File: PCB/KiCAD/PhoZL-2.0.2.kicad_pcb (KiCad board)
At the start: 2 copper layers, 125.5 x 90.3 mm, 106 parts, among them J1 Conn_01x06_Female, J11 Conn_01x02, J14 Conn_01x06, J15 Conn_01x06, J2 Conn_01x02, J3 Conn_01x02, J4 Conn_01x01, J5 Rumble, J6 Conn_01x06, J8 USB_B_Micro, Q1 Q_NMOS_GSD, Q2 Q_PMOS_GDS, Q3 Q_NMOS_GSD, SW1 A, SW10 Dup, SW11 Dright, SW12 Ddown, SW2 B, SW3 X, SW4 Y, SW5 Start, SW6 L, SW7 R, SW8 ZR, SW8L ZL, SW9 Dleft, U1 MCP3002, U10 DRV5055A2xDBZxQ1, U11 DRV5055A2xDBZxQ1, U2 Stickbox_Assembly_Main, U3 MCP3002, U4 DRV5055A2xDBZxQ1, U5 Stickbox_Assembly_CStick, U6 AMS1117-3.3, U7 W25Q128JVS, U8 RP2040, U9 DRV5055A2xDBZxQ1, Y1 Crystal_GND24

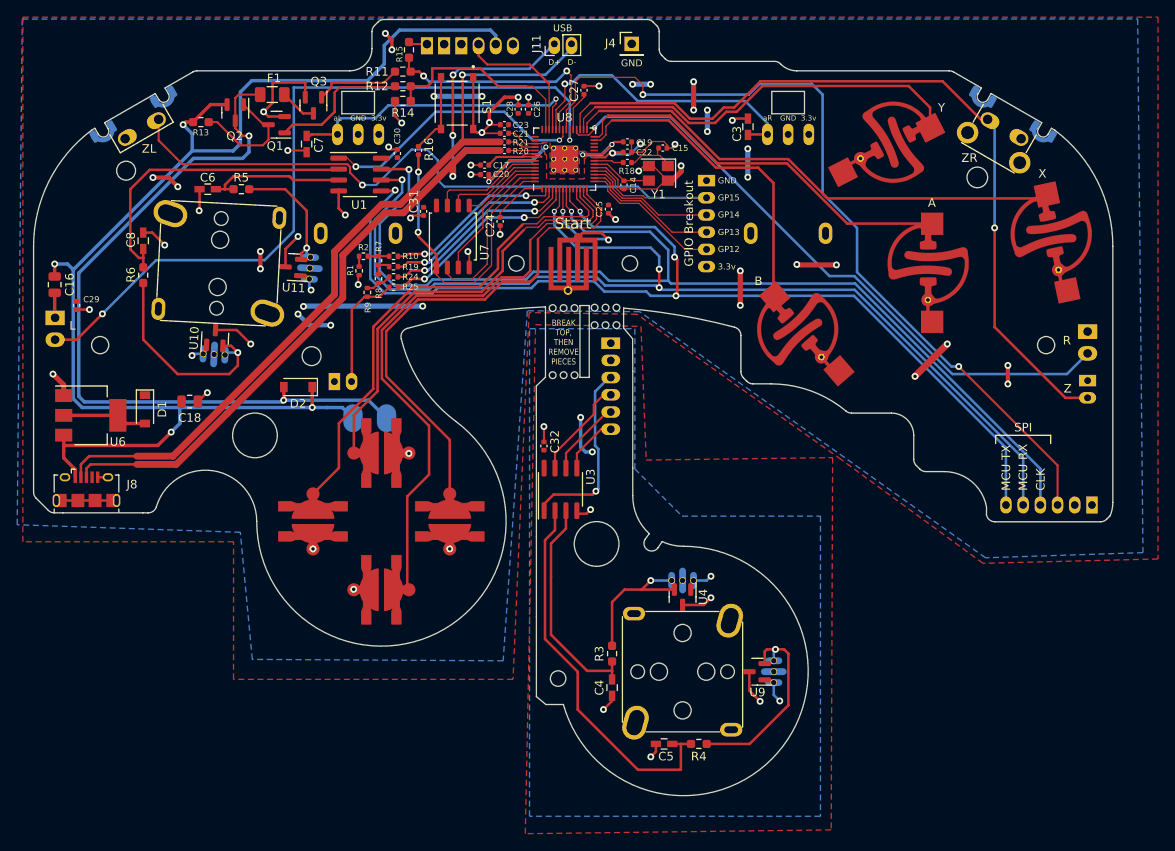
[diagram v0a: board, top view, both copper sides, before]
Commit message: 12-16-22 Changes
pcb has been redone on the newest version of the 2.0.2 pcb
(my dpad was added to the main pcb!)
gpio15 on zl changed to gpio12
removed the zl input from the GPIO breakout, instead going directly into the rp2040
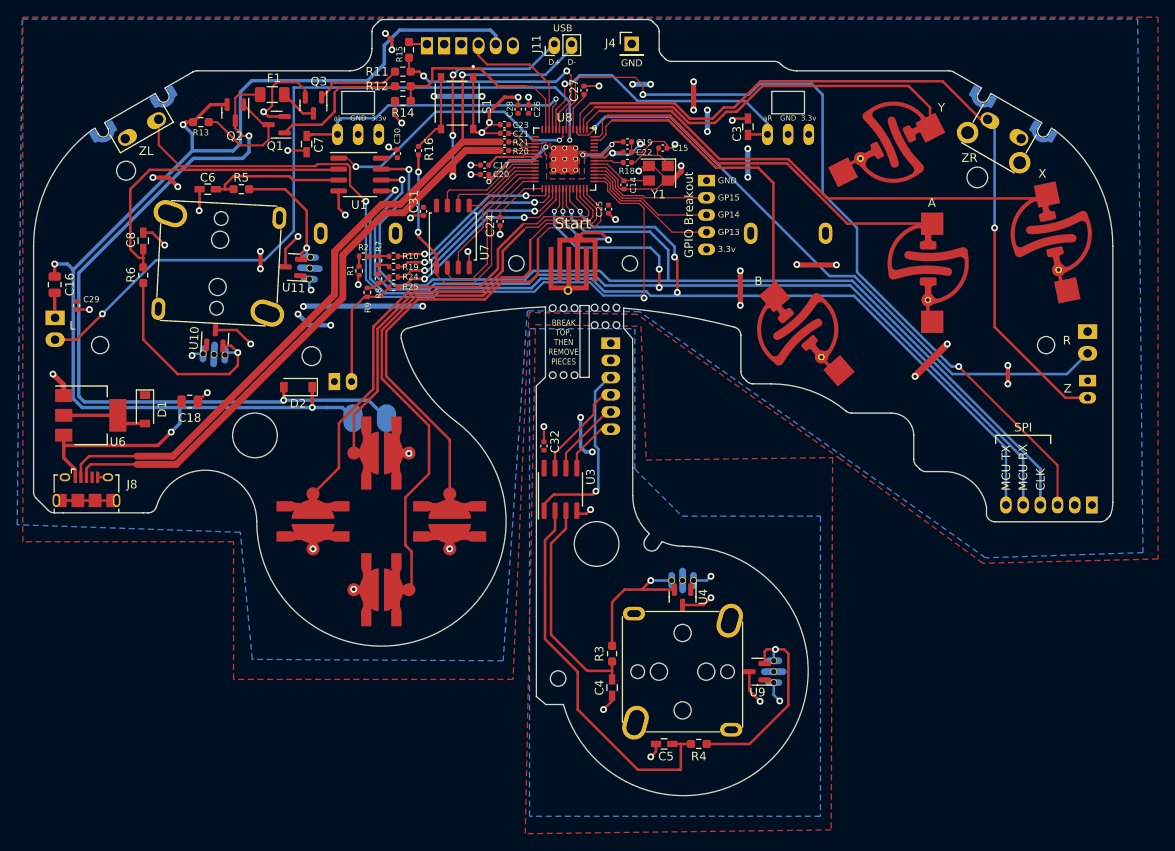
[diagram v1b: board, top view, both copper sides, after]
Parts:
- SW8: value ZR -> Z
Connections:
- J6 pad 2: /GPIO12 -> +3V3
- SW8L pad 2: /GPIO15 -> /GPIO12
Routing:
- net /GPIO12: track 17.0 -> 92.9 mm, vias 0 -> 2
- net /GPIO15: track 89.1 -> 15.0 mm, vias 1 -> 0
- net /Din: track 124.9 -> 125.7 mm
- net GND: track 138.4 -> 137.8 mm
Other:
- board text removed: "GP12"

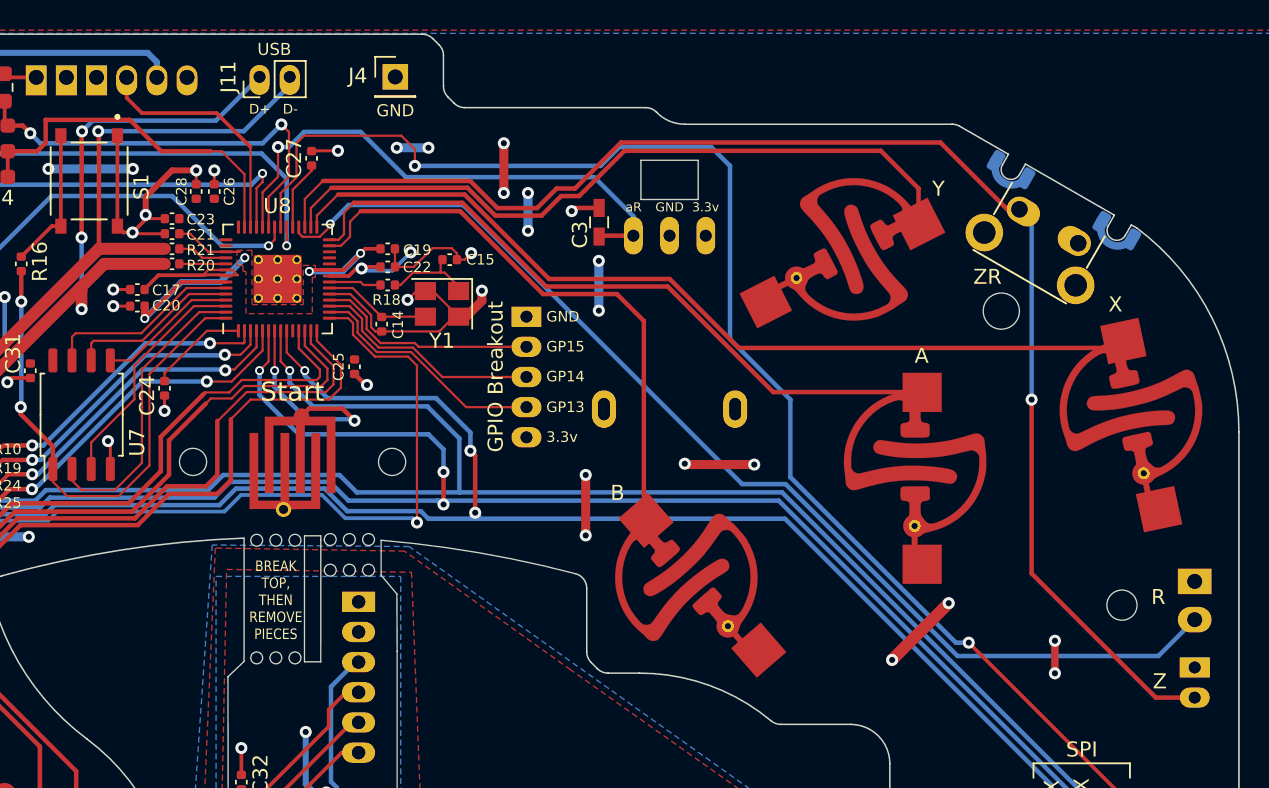
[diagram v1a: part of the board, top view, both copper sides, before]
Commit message: 12-20-22 Changes
slight updates to the silkscreen
USB Data + / - as well as the GND at the top of the PCB has been relocated
(Credit to Plants for the idea!)
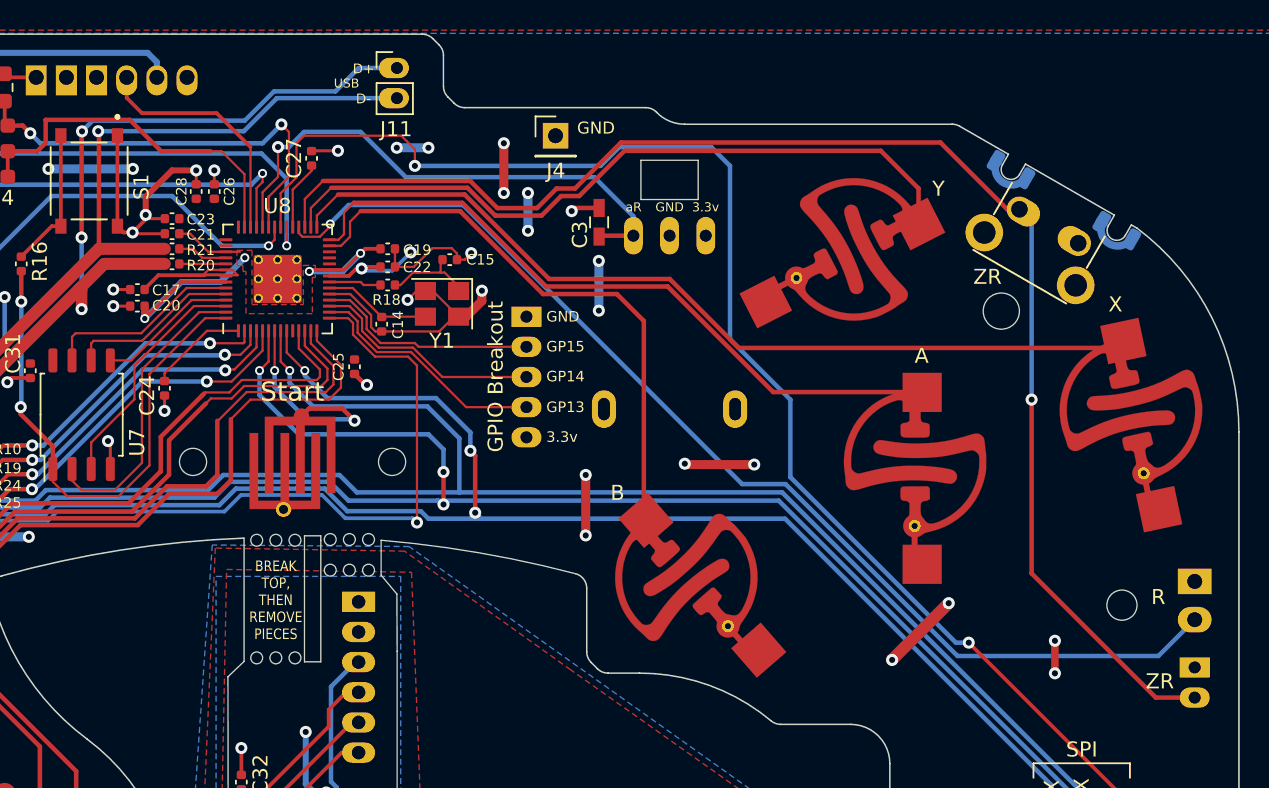
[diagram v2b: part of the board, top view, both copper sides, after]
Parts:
- moved J4 11.3 mm to (128.4, 29.6)
- moved J11 9.13 mm to (117.9, 25.0), turned to 0 degrees
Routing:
- net /USB_D+: track 93.9 -> 103.2 mm
- net /USB_D-: track 91.1 -> 97.3 mm
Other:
- board text removed: "Z"
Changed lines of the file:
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@@
   )
   (footprint "PhobGCC_2_0_0_footprints:PinHeader_1x01_P2.54mm_Vertical" (layer "F.Cu")
-    (at 117.8 25.6)
+    (at 128.43 29.55)
     (descr "Through hole straight pin header, 1x01, 2.54mm pitch, single row")
     (tags "Through hole pin header THT 1x01 2.54mm single row")
@@
     (property "Sheetname" "")
     (attr through_hole)
-    (fp_text reference "J4" (at -2.484 -0.073) (layer "F.SilkS")
+    (fp_text reference "J4" (at 0.02 2.28) (layer "F.SilkS")
       (effects (font (size 1 1) (thickness 0.15)))
     )
@@
     (fp_line (start 1.27 1.27) (end -1.27 1.27) (layer "F.Fab") (width 0.1))
     (fp_line (start -1.27 -0.635) (end -0.635 -1.27) (layer "F.Fab") (width 0.1))
-    (pad "1" thru_hole rect (at 0 0) (size 1.7 1.7) (drill 1) (layers *.Cu *.Mask)
+    (pad "1" thru_hole rect (at 0 -0.05) (size 1.7 1.7) (drill 1) (layers *.Cu *.Mask)
       (net 1 "GND") (pinfunction "Pin_1") (pintype "passive"))
     (model "${KICAD6_3DMODEL_DIR}/Connector_PinHeader_2.54mm.3dshapes/PinHeader_1x01_P2.54mm_Vertical.wrl" hide
@@
   )
   (footprint "PhobGCC_2_0_0_footprints:PinHeader_1x02_P2.00mm_Vertical" (layer "F.Cu")
-    (at 108.8 25.6 90)
+    (at 117.91 25.01)
     (descr "Through hole straight pin header, 1x02, 2.00mm pitch, single row")
     (tags "Through hole pin header THT 1x02 2.00mm single row")
@@
     (property "Sheetname" "")
     (attr through_hole)
-    (fp_text reference "J11" (at 0 -2.06 90) (layer "F.SilkS")
+    (fp_text reference "J11" (at -0.05 4.06) (layer "F.SilkS")
       (effects (font (size 1 1) (thickness 0.15)))
     )
-    (fp_text value "Conn_01x02" (at 0 4.06 90) (layer "F.Fab")
+    (fp_text value "Conn_01x02" (at 0 4.06) (layer "F.Fab")
       (effects (font (size 1 1) (thickness 0.15)))
     )
-    (fp_text user "${REFERENCE}" (at 0 1) (layer "F.Fab")
+    (fp_text user "${REFERENCE}" (at 0 1 90) (layer "F.Fab")
       (effects (font (size 1 1) (thickness 0.15)))
     )
@@
     (fp_line (start 1 3) (end -1 3) (layer "F.Fab") (width 0.1))
     (fp_line (start -0.5 -1) (end 1 -1) (layer "F.Fab") (width 0.1))
-    (pad "1" thru_hole oval (at 0 0 90) (size 2 1.35) (drill 0.8 (offset -0.2 0)) (layers *.Cu *.Mask)
+    (pad "1" thru_hole oval (at 0 0) (size 2 1.35) (drill 0.8 (offset -0.2 0)) (layers *.Cu *.Mask)
       (net 37 "/USB_D+") (pinfunction "Pin_1") (pintype "passive"))
-    (pad "2" thru_hole oval (at 0 2 90) (size 2 1.35) (drill 0.8 (offset -0.2 0)) (layers *.Cu *.Mask)
+    (pad "2" thru_hole oval (at 0 2) (size 2 1.35) (drill 0.8 (offset -0.2 0)) (layers *.Cu *.Mask)
       (net 38 "/USB_D-") (pinfunction "Pin_2") (pintype "passive"))
     (model "${KICAD6_3DMODEL_DIR}/Connector_PinHeader_2.00mm.3dshapes/PinHeader_1x02_P2.00mm_Vertical.wrl" hide
@@
     (effects (font (size 0.7 0.7) (thickness 0.15)) (justify right mirror))
   )
-  (gr_text "Z" (at 168.5036 65.6844) (layer "B.SilkS")
+  (gr_text "ZR" (at 168.5036 65.6844) (layer "B.SilkS")
     (effects (font (size 1 1) (thickness 0.15)) (justify mirror))
   )
@@
     (effects (font (size 0.6 0.6) (thickness 0.1)))
   )
-  (gr_text "D-" (at 110.8436 27.7368) (layer "F.SilkS")
+  (gr_text "D-" (at 115.69 27.05) (layer "F.SilkS")
     (effects (font (size 0.65 0.65) (thickness 0.15)))
   )
@@
     (effects (font (size 1 1) (thickness 0.15)) (justify left))
   )
-  (gr_text "D+" (at 108.8136 27.7368) (layer "F.SilkS")
+  (gr_text "D+" (at 115.69 25.06) (layer "F.SilkS")
     (effects (font (size 0.65 0.65) (thickness 0.15)))
   )
@@
     (effects (font (size 1 1) (thickness 0.15)) (justify left))
   )
-  (gr_text "Z" (at 168.5036 65.6844) (layer "F.SilkS")
+  (gr_text "ZR" (at 168.5036 65.6844) (layer "F.SilkS")
     (effects (font (size 1 1) (thickness 0.15)))
   )
@@
     (effects (font (size 0.7 0.7) (thickness 0.15)) (justify left))
   )
-  (gr_text "GND" (at 117.8052 27.8384) (layer "F.SilkS")
+  (gr_text "GND" (at 131.11 28.99) (layer "F.SilkS")
     (effects (font (size 0.8 0.8) (thickness 0.15)))
   )
@@
     (effects (font (size 1 1) (thickness 0.15)))
   )
-  (gr_text "USB" (at 109.7788 23.7744) (layer "F.SilkS")
-    (effects (font (size 0.8 0.8) (thickness 0.15)))
+  (gr_text "USB" (at 114.57 26.03) (layer "F.SilkS")
+    (effects (font (size 0.6 0.6) (thickness 0.1125)))
   )
   (gr_text "SPI" (at 163.322 70.2056) (layer "F.SilkS")
@@
   (segment (start 97 41) (end 97 36.25) (width 0.3) (layer "B.Cu") (net 37))
   (segment (start 97.028 29.21) (end 97.738 28.5) (width 0.3) (layer "B.Cu") (net 37))
-  (segment (start 105.9 28.5) (end 108.8 25.6) (width 0.3) (layer "B.Cu") (net 37))
-  (segment (start 97.738 28.5) (end 105.9 28.5) (width 0.3) (layer "B.Cu") (net 37))
+  (segment (start 107.820404 28.5) (end 109.760404 26.56) (width 0.3) (layer "B.Cu") (net 37))
+  (segment (start 109.760404 26.56) (end 113.83 26.56) (width 0.3) (layer "B.Cu") (net 37))
+  (segment (start 113.83 26.56) (end 115.38 25.01) (width 0.3) (layer "B.Cu") (net 37))
+  (segment (start 97.738 28.5) (end 107.820404 28.5) (width 0.3) (layer "B.Cu") (net 37))
+  (segment (start 115.38 25.01) (end 117.91 25.01) (width 0.3) (layer "B.Cu") (net 37))
   (segment (start 64.45452 73.54548) (end 83.25 54.75) (width 0.8) (layer "F.Cu") (net 38))
   (segment (start 60.25 73.54548) (end 64.45452 73.54548) (width 0.8) (layer "F.Cu") (net 38))
@@
   (segment (start 54.70452 73.54548) (end 60.25 73.54548) (width 0.3) (layer "F.Cu") (net 38))
   (via (at 98.1 29.2) (size 0.8) (drill 0.4) (layers "F.Cu" "B.Cu") (net 38))
-  (segment (start 107.7568 29.2) (end 110.8 26.1568) (width 0.3) (layer "B.Cu") (net 38))
-  (segment (start 110.8 26.1568) (end 110.8 25.6) (width 0.3) (layer "B.Cu") (net 38))
   (segment (start 98.1 29.2) (end 107.7568 29.2) (width 0.3) (layer "B.Cu") (net 38))
+  (segment (start 107.7568 29.2) (end 109.9468 27.01) (width 0.3) (layer "B.Cu") (net 38))
+  (segment (start 109.9468 27.01) (end 117.91 27.01) (width 0.3) (layer "B.Cu") (net 38))
   (segment (start 93 37.52) (end 95.02 35.5) (width 0.25) (layer "F.Cu") (net 39))
   (segment (start 95.625 29.5) (end 95.625 35.5) (width 0.25) (layer "F.Cu") (net 39))

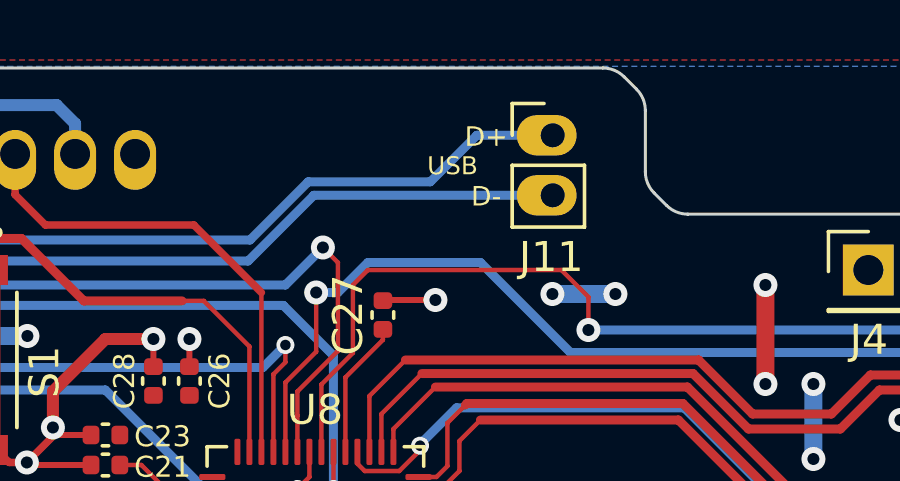
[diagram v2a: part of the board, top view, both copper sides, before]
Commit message: 12-23-22 Changes
updated dpad to match current phob 2
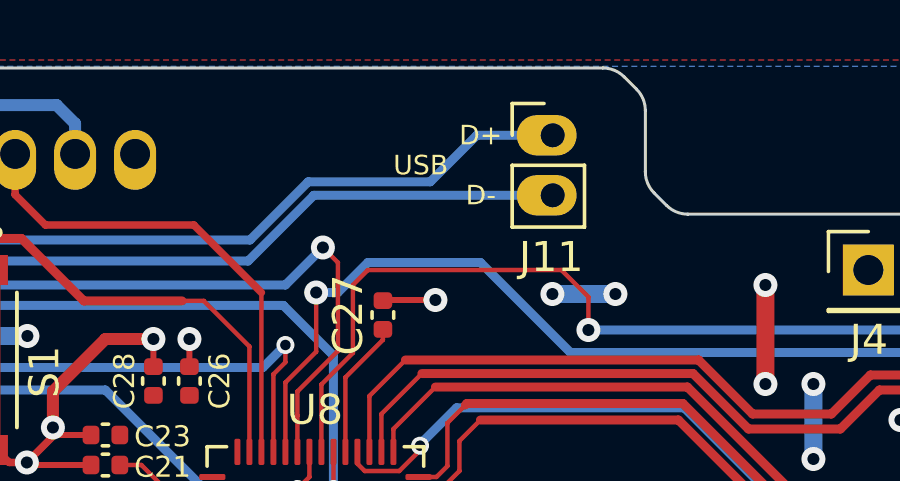
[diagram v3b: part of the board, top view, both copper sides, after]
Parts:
- SW10, SW11, SW12, SW9: footprint PhobGCC_2_0_0_footprints:Dpad_Contact_TL3315NF_2 -> ssimages:Dpad_Contact_TL3315NF_2
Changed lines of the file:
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@@
       (drillshape 0)
       (scaleselection 1)
-      (outputdirectory "../../../../PhobGCCv2-Production_Files/")
+      (outputdirectory "../../../!PhoZL Dpad Edit Gerbers/")
     )
   )
@@
     (pad "MP" thru_hole circle (at -3.5 2.5 330) (size 2.5 2.5) (drill 1.5) (layers *.Cu *.Mask))
   )
-  (footprint "PhobGCC_2_0_0_footprints:Dpad_Contact_TL3315NF_2" (layer "F.Cu")
+  (footprint "ssimages:Dpad_Contact_TL3315NF_2" (layer "F.Cu")
     (at 80.74 81.13 180)
     (property "Sheetfile" "File: PhobGCC_2_0_0_proto_1.kicad_sch")
@@
           ) (width 0.1) (fill yes))
       ))
+    (zone (net 0) (net_name "") (layer "F.Cu") (hatch edge 0.508)
+      (connect_pads (clearance 0))
+      (min_thickness 0.254)
+      (keepout (tracks allowed) (vias allowed) (pads allowed) (copperpour not_allowed) (footprints allowed))
+      (fill (thermal_gap 0.508) (thermal_bridge_width 0.508))
+      (polygon
+        (pts
+          (xy 77.74 79.83)
+          (xy 83.74 79.83)
+          (xy 83.74 82.43)
+          (xy 77.74 82.43)
+        )
+      )
+    )
   )
-  (footprint "PhobGCC_2_0_0_footprints:Dpad_Contact_TL3315NF_2" (layer "F.Cu")
+  (footprint "ssimages:Dpad_Contact_TL3315NF_2" (layer "F.Cu")
     (at 88.69 73.18 -90)
     (property "Sheetfile" "File: PhobGCC_2_0_0_proto_1.kicad_sch")
@@
           ) (width 0.1) (fill yes))
       ))
+    (zone (net 0) (net_name "") (layer "F.Cu") (hatch edge 0.508)
+      (connect_pads (clearance 0))
+      (min_thickness 0.254)
+      (keepout (tracks allowed) (vias allowed) (pads allowed) (copperpour not_allowed) (footprints allowed))
+      (fill (thermal_gap 0.508) (thermal_bridge_width 0.508))
+      (polygon
+        (pts
+          (xy 87.39 76.18)
+          (xy 87.39 70.18)
+          (xy 89.99 70.18)
+          (xy 89.99 76.18)
+        )
+      )
+    )
   )
-  (footprint "PhobGCC_2_0_0_footprints:Dpad_Contact_TL3315NF_2" (layer "F.Cu")
+  (footprint "ssimages:Dpad_Contact_TL3315NF_2" (layer "F.Cu")
     (at 96.64 81.13 180)
     (property "Sheetfile" "File: PhobGCC_2_0_0_proto_1.kicad_sch")
@@
       (effects (font (size 1.27 1.27) (thickness 0.15)))
     )
-    (fp_circle (center 0 0) (end 2.53 -0.05) (layer "F.Mask") (width 0.12) (fill solid))
     (fp_circle (center 0 -3.2) (end 0.75 -3.18) (layer "F.Mask") (width 0.12) (fill solid))
+    (fp_circle (center 0 0) (end 2.53 -0.05) (layer "F.Mask") (width 0.12) (fill solid))
     (fp_circle (center 0 3.2) (end 0.75 3.12) (layer "F.Mask") (width 0.12) (fill solid))
     (fp_circle (center 0 0) (end 0 -2.5) (layer "Dwgs.User") (width 0.12) (fill none))
@@
           ) (width 0.1) (fill yes))
       ))
+    (zone (net 0) (net_name "") (layer "F.Cu") (hatch edge 0.508)
+      (connect_pads (clearance 0))
+      (min_thickness 0.254)
+      (keepout (tracks allowed) (vias allowed) (pads allowed) (copperpour not_allowed) (footprints allowed))
+      (fill (thermal_gap 0.508) (thermal_bridge_width 0.508))
+      (polygon
+        (pts
+          (xy 93.64 79.83)
+          (xy 99.64 79.83)
+          (xy 99.64 82.43)
+          (xy 93.64 82.43)
+        )
+      )
+    )
   )
-  (footprint "PhobGCC_2_0_0_footprints:Dpad_Contact_TL3315NF_2" (layer "F.Cu")
+  (footprint "ssimages:Dpad_Contact_TL3315NF_2" (layer "F.Cu")
     (at 88.69 89.08 90)
     (property "Sheetfile" "File: PhobGCC_2_0_0_proto_1.kicad_sch")
@@
     )
     (fp_circle (center 0 0) (end 2.53 -0.05) (layer "F.Mask") (width 0.12) (fill solid))
-    (fp_circle (center 0 3.2) (end 0.75 3.12) (layer "F.Mask") (width 0.12) (fill solid))
     (fp_circle (center 0 -3.2) (end 0.75 -3.18) (layer "F.Mask") (width 0.12) (fill solid))
+    (fp_circle (center 0 3.2) (end 0.75 3.12) (layer "F.Mask") (width 0.12) (fill solid))
     (fp_circle (center 0 0) (end 0 -2.5) (layer "Dwgs.User") (width 0.12) (fill none))
     (pad "1" smd custom (at 0 3.2 90) (size 1.524 1.524) (layers "F.Cu" "F.Paste" "F.Mask")
@@
           ) (width 0.1) (fill yes))
       ))
+    (zone (net 0) (net_name "") (layer "F.Cu") (hatch edge 0.508)
+      (connect_pads (clearance 0))
+      (min_thickness 0.254)
+      (keepout (tracks allowed) (vias allowed) (pads allowed) (copperpour not_allowed) (footprints allowed))
+      (fill (thermal_gap 0.508) (thermal_bridge_width 0.508))
+      (polygon
+        (pts
+          (xy 89.99 86.08)
+          (xy 89.99 92.08)
+          (xy 87.39 92.08)
+          (xy 87.39 86.08)
+        )
+      )
+    )
   )
   (footprint "PhobGCC_2_0_0_footprints:GCC_Stickbox_Hall_Only" (layer "F.Cu")
@@
     (effects (font (size 0.6 0.6) (thickness 0.1)))
   )
-  (gr_text "D-" (at 115.69 27.05) (layer "F.SilkS")
+  (gr_text "D-" (at 115.51 27.01) (layer "F.SilkS")
     (effects (font (size 0.65 0.65) (thickness 0.15)))
   )
@@
     (effects (font (size 1 1) (thickness 0.15)) (justify left))
   )
-  (gr_text "D+" (at 115.69 25.06) (layer "F.SilkS")
+  (gr_text "D+" (at 115.51 25.01) (layer "F.SilkS")
     (effects (font (size 0.65 0.65) (thickness 0.15)))
   )
@@
     (effects (font (size 1 1) (thickness 0.15)))
   )
-  (gr_text "USB" (at 114.57 26.03) (layer "F.SilkS")
-    (effects (font (size 0.6 0.6) (thickness 0.1125)))
+  (gr_text "USB" (at 113.51 26.01) (layer "F.SilkS")
+    (effects (font (size 0.65 0.65) (thickness 0.15)))
   )
   (gr_text "SPI" (at 163.322 70.2056) (layer "F.SilkS")
